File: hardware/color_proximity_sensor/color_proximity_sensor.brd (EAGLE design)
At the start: 48 x 24.8 mm, 69 parts, among them IC1 TCS37725FN, IC2 APDS-9800-021, IC4 LM25011MY, IC5 ATXMEGA64D4-AU, J1 PDI_ATMEL_WIDTH, Q1 16 MHz, T1 BC847CDXV6T1G, T4 BC847CDXV6T1G

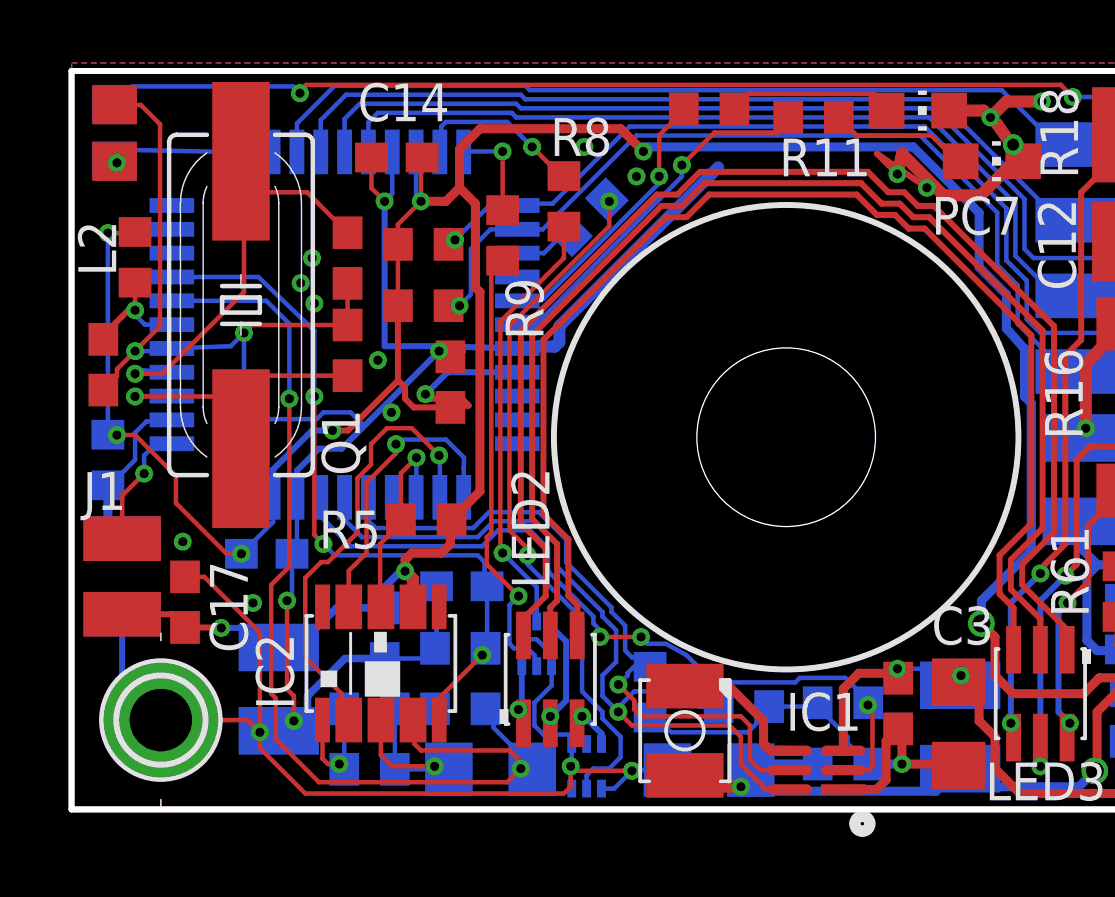
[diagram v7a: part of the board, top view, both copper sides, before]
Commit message: color_proximity_sensor : VL53L0X sensor integrated
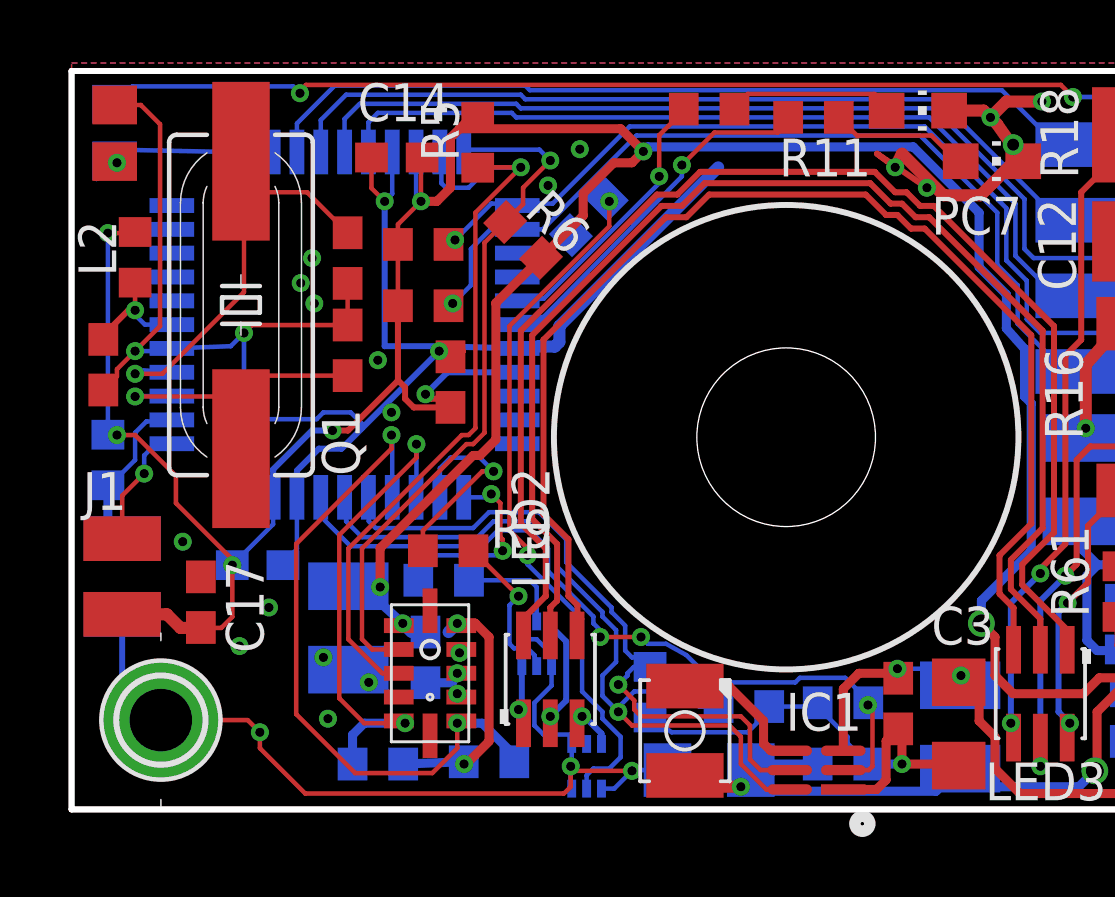
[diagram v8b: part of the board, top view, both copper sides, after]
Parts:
- removed C6: 22µF 10V, robotter_capacitor:C1210
- removed C7, C8: 100nF 50V, robotter_capacitor:C0603
- removed C9: 1µF 25V, robotter_capacitor:C1206
- removed IC2: APDS-9800-021, robotter_ic:APDS-9800
- removed R7: 15k 1%, robotter_resistor:R0603
- added C20: 10µF 25V, robotter_capacitor:C1210
- added C21: 100nF 50V, robotter_capacitor:C0603
- added IC3: VL53L0x, robotter_ic:LGA12
- R3, R4: value 22 ohms -> 10K-F
- R5: value 10K-F -> 3K09-F
- R6: value 1k -> 3K09-F
- moved R6 15.9 mm to (15.2, 19.1), flipped to the top, turned to 315 degrees
- moved R8 13.4 mm to (12.5, 7.70), flipped to the bottom, turned to 180 degrees
- moved R5 12.8 mm to (13.6, 22.4), turned to 90 degrees
- moved R9 10.7 mm to (12.6, 8.69), turned to 0 degrees
- moved R3 4.39 mm to (14.0, 1.60)
- moved C17 0.53 mm to (4.34, 6.96)
- moved C16 0.49 mm to (6.25, 8.20)
- moved R4 0.33 mm to (10.3, 1.52), turned to 180 degrees
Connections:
- removed net APDS_AMBIENT_0-300MV: C9.2, IC2.7, IC5.40, R6.2
- removed net APDS_ENABLE_3V3: IC2.9, IC5.24
- removed net APDS_LED_PWM_3V3: IC2.2, IC5.23
- removed net APDS_OUTPUT_3V3: IC2.3, IC5.25, R5.1
- removed net APDS_PROXIMITY_ANA_0-0.65V: C8.2, IC2.6, IC5.41, R7.2
- removed net N$2: IC2.10, R3.2, R4.2
- new net CE_VL53L0X_3V3: IC3.5, IC5.26, R3.1
- new net INT_VL53L0X_3V3: IC3.7, IC5.25, R4.1
- new net SCL_VL53V0X_3V3: IC3.10, IC5.11, R6.1
- new net SDA_VL53V0X_3V3: IC3.9, IC5.10, R5.1
- net +3V3: now also C20.1, C21.1, IC3.1, IC3.11, R3.2, R4.2, R6.2; no longer C6.1, C7.1, IC2.4
- net GND: now also C20.2, C21.2, IC3.12, IC3.2, IC3.3, IC3.4, IC3.6; no longer C6.2, C7.2, C8.1, C9.1, IC2.8, R3.1, R4.1, R6.1, R7.1
- net LED_BLUE_CMD_3V3: now also IC5.23; no longer IC5.10
- net LED_GREEN_CMD_3V3: now also IC5.24; no longer IC5.11
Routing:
- net APDS_AMBIENT_0-300MV: track 35.6 -> 0.00 mm, vias 2 -> 0
- net GND: track 223.0 -> 191.1 mm, vias 38 -> 42
- net SDA_VL53V0X_3V3: track 0.00 -> 26.1 mm, vias 0 -> 1
- net APDS_PROXIMITY_ANA_0-0.65V: track 25.3 -> 0.00 mm, vias 3 -> 0
- net SCL_VL53V0X_3V3: track 0.00 -> 23.3 mm, vias 0 -> 1
- net CE_VL53L0X_3V3: track 0.00 -> 23.0 mm, vias 0 -> 2
- net INT_VL53L0X_3V3: track 0.00 -> 17.3 mm, vias 0 -> 2
- net APDS_ENABLE_3V3: track 15.4 -> 0.00 mm, vias 1 -> 0
- net N$1: track 14.6 -> 3.52 mm, vias 1 -> 0
- net APDS_LED_PWM_3V3: track 10.1 -> 0.00 mm, vias 1 -> 0
- net +3V3: track 148.3 -> 157.5 mm, vias 12 -> 14
- net N$3: track 15.2 -> 6.25 mm
- net APDS_OUTPUT_3V3: track 6.95 -> 0.00 mm, vias 1 -> 0
- net N$2: track 4.45 -> 0.00 mm, vias 1 -> 0
- net LED_GREEN_CMD_3V3: track 3.28 -> 6.99 mm
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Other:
- board text added: "color_prox sens v3"
- board text removed: "color_prox sens v2"
